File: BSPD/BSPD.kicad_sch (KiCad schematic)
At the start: 54 parts, among them J1 DT13-48PABCD-R015, K1 Latching Relay, Q2 STS6NF20V, Q3 STS6NF20V, U1 LM7805CT, U10 DK1A1B-12V, U12 OP AMP, U14 ISO1050DUB, U15 LM7809_TO220, U2 NSL-32, U2 OP AMP, U3 OP AMP, U4 NUCLEO-L432KC, U5 2x4 OR GATE, U6 LM555N, U8 NAND, U9 AND GATE

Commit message: Finished slug logo and shrunk pcb to size of components
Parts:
- removed SYM1: SYM_EasterEgg_42x60mm, 1FS_2_Global_Footprint_Library:FORMULA SLUG, symbol Graphic:SYM_EasterEgg_42x60mm
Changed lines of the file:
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@@
   (title_block
     (title "Brake System Plausability Device +")
-    (date "2024-02-22")
+    (date "2024-02-27")
     (rev "FS2 4.3")
   )
@@
     )
   )
+  (symbol (lib_id "1FS_2_Global_Symbol_Library:FS Logo") (at 535.94 44.45 0) (unit 1)
+    (in_bom yes) (on_board yes) (dnp no) (fields_autoplaced)
+    (property "Reference" "#G1" (at 535.94 19.685 0)
+      (effects (font (size 1.27 1.27)) hide)
+    )
+    (property "Value" "FS Logo" (at 535.94 69.215 0)
+      (effects (font (size 1.27 1.27)) hide)
+    )
+    (property "Footprint" "1FS_2_Global_Footprint_Library:FORMULA SLUG" (at 535.94 44.45 0)
+      (effects (font (size 1.27 1.27)) hide)
+    )
+    (property "Datasheet" "" (at 535.94 44.45 0)
+      (effects (font (size 1.27 1.27)) hide)
+    )
+    (instances
+      (project "BSPD"
+        (path "/9b958334-fa88-4811-8197-71444a07b1b5"
+          (reference "#G1") (unit 1)
+        )
+      )
+    )
+  )
   (symbol (lib_id "Device:R_US") (at 119.38 50.8 270) (unit 1)
     (in_bom yes) (on_board yes) (dnp no)
@@
         )
       )
-    )
-  )
-  (symbol (lib_id "Graphic:SYM_EasterEgg_42x60mm") (at 548.64 86.36 0) (unit 1)
-    (in_bom no) (on_board yes) (dnp no) (fields_autoplaced)
-    (property "Reference" "SYM1" (at 548.64 86.36 0)
-      (effects (font (size 1.27 1.27)) hide)
-    )
-    (property "Value" "SYM_EasterEgg_42x60mm" (at 548.64 86.36 0)
-      (effects (font (size 1.27 1.27)) hide)
-    )
-    (property "Footprint" "1FS_2_Global_Footprint_Library:FORMULA SLUG" (at 548.64 90.17 0)
-      (effects (font (size 1.27 1.27)) hide)
-    )
-    (property "Datasheet" "https://eur-lex.europa.eu/LexUriServ/LexUriServ.do?uri=OJ:L:2013:347:0671:0854:de:PDF" (at 548.64 92.71 0)
-      (effects (font (size 1.27 1.27)) hide)
-    )
-    (property "Sim.Enable" "0" (at 548.64 88.9 0)
-      (effects (font (size 1.27 1.27)) hide)
-    )
-    (instances
-      (project "BSPD"
-        (path "/9b958334-fa88-4811-8197-71444a07b1b5"
-          (reference "SYM1") (unit 1)
-        )
-      )

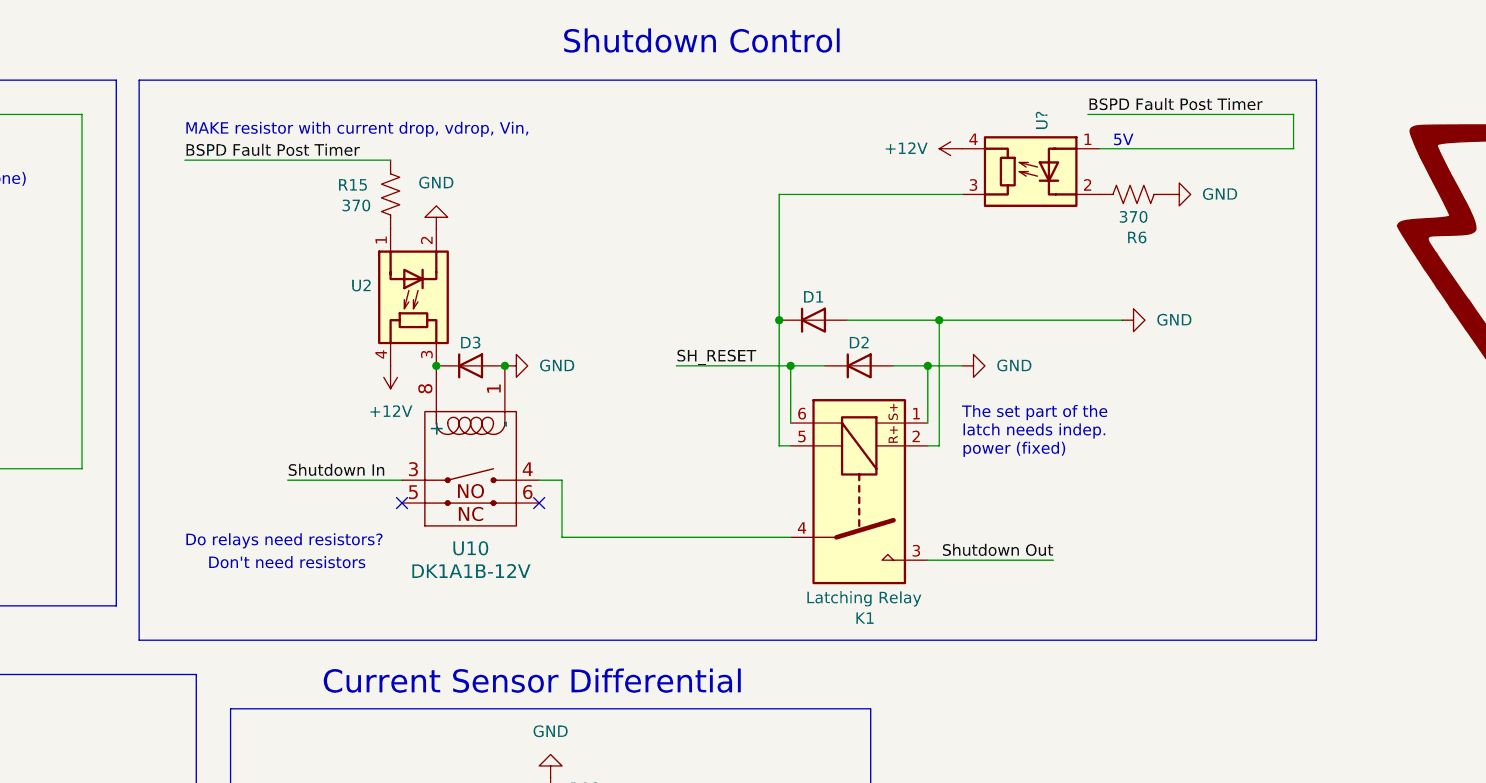
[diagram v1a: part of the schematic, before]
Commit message: Fixed stray traces, optocoupler pins, and opto library entry
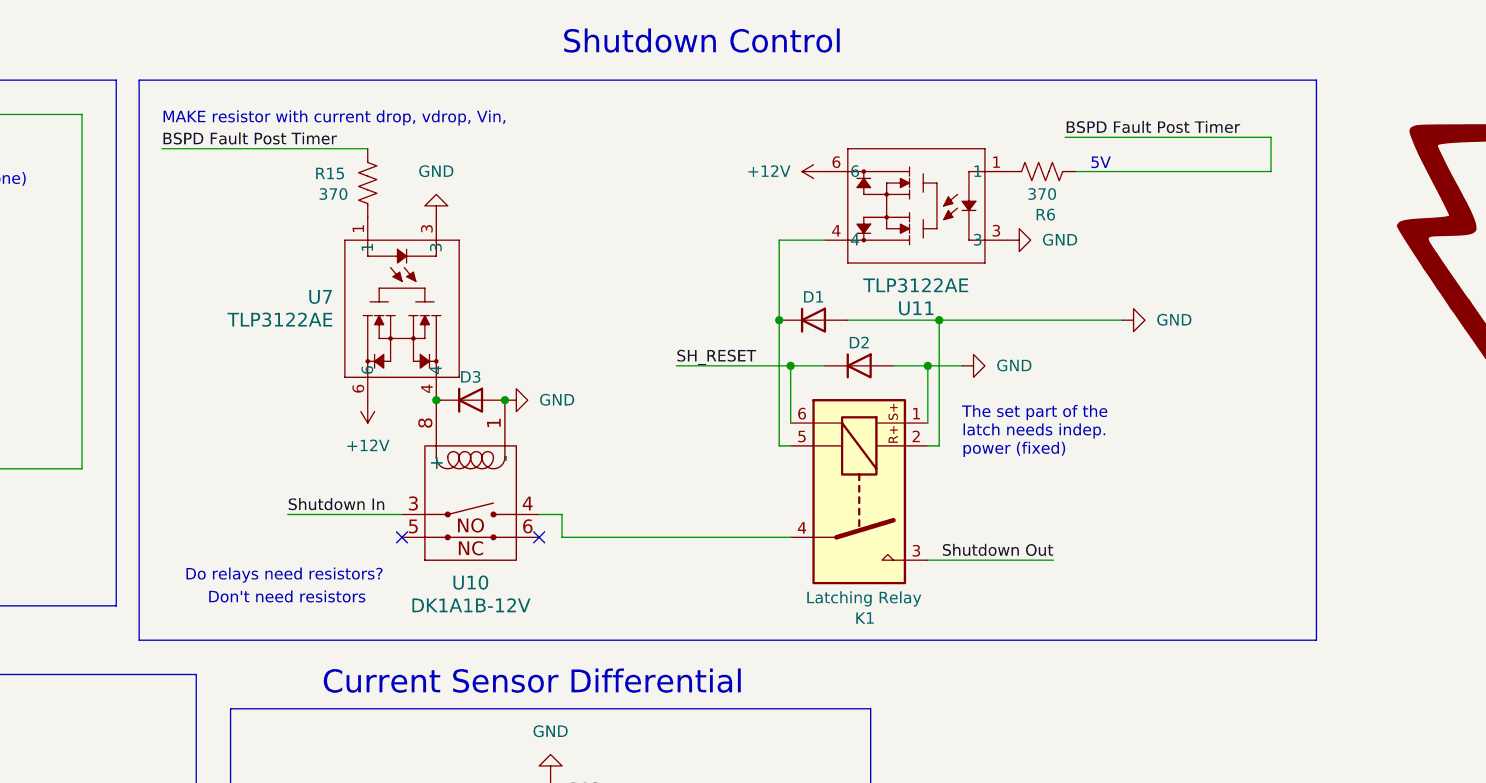
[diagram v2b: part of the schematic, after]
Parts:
- removed U2, U?: NSL-32, 1FS_2_Global_Footprint_Library:OptoCoupler 6-SOP, symbol Isolator:NSL-32
- added U11, U7: TLP3122AE, 1FS_2_Global_Footprint_Library:OptoCoupler 6-SOP, symbol 1FS_2_Global_Symbol_Library:TLP3122AE
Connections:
- net +12V: now also U11.6, U7.6
- net BSPD Fault Post Timer: now also R6.1
- net GND: now also U11.3, U7.3; no longer R6.1
- net at R15.1: now also U7.1
- net at D3.1 (K), U10.8 (+): now also U7.4
- net at D1.1 (K), K1.5: now also U11.4
- net at R6.2: now also U11.1
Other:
- moved on the sheet: D3, R15, R6, U10

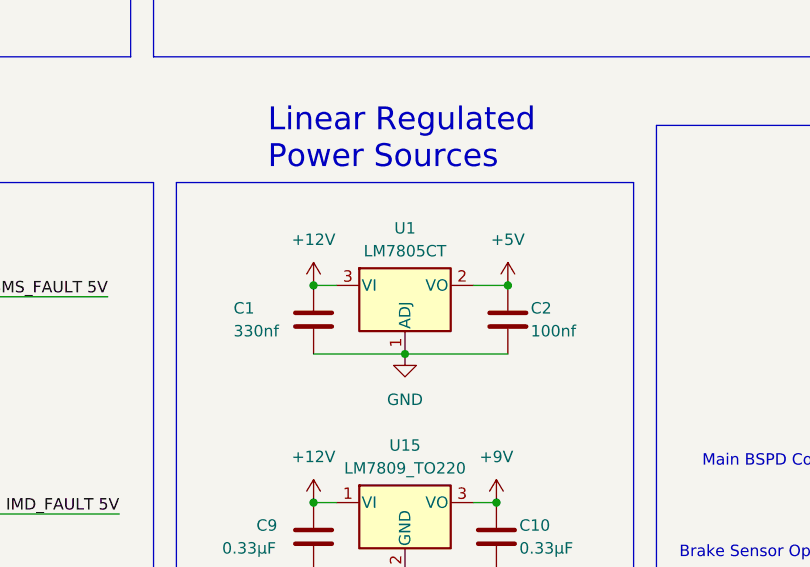
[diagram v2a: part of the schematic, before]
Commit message: fixed 5v lin reg pins and trace overlapping holes
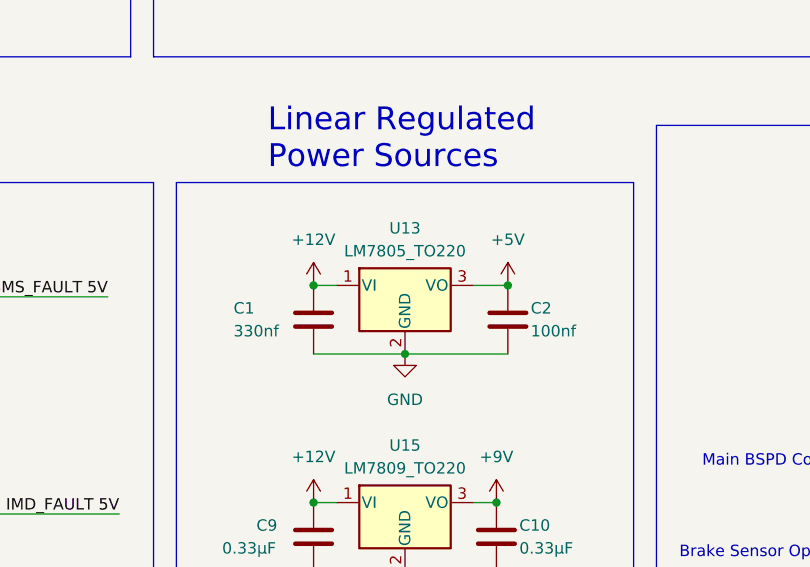
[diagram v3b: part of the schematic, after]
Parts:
- removed U1: LM7805CT, Package_TO_SOT_THT:TO-220-3_Vertical, symbol Regulator_Linear:LM317_TO-252
- added U13: LM7805_TO220, Package_TO_SOT_THT:TO-220-3_Vertical, symbol Regulator_Linear:LM7805_TO220
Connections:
- net +12V: now also U13.1 (VI)
- net +5V: now also U13.3 (VO)
- net GND: now also U13.2 (GND)

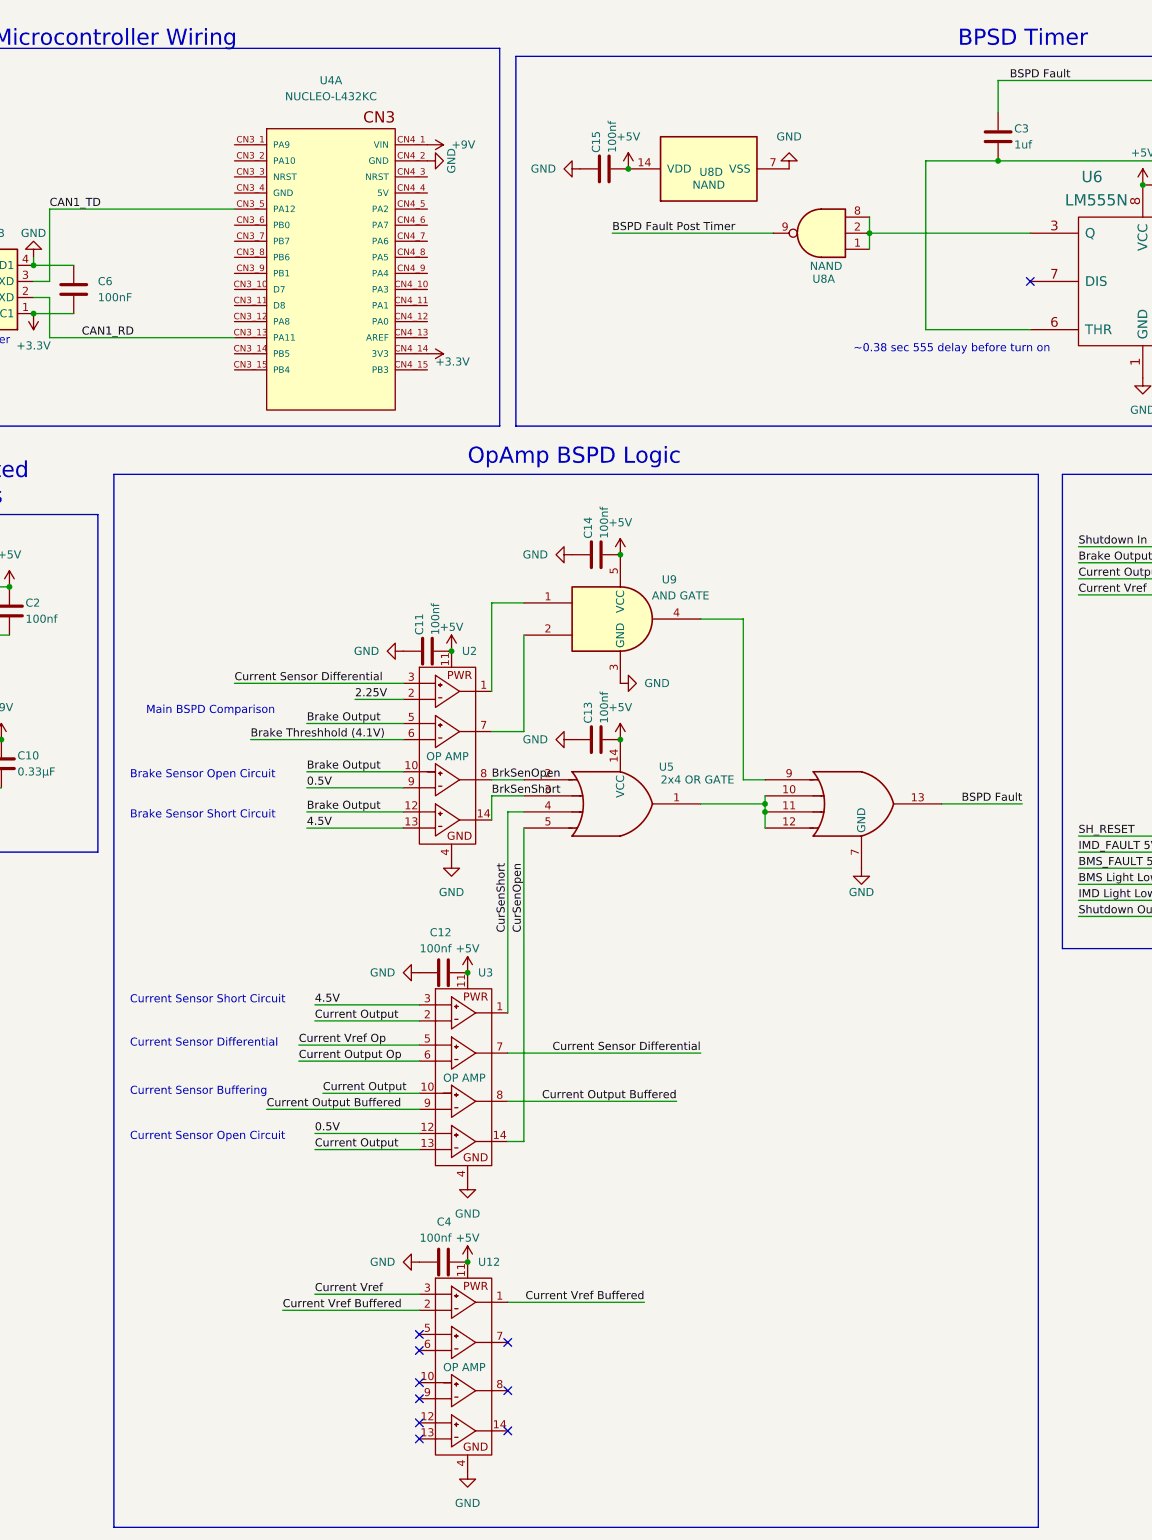
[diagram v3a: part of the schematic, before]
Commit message: fixed and/nand pins and packages
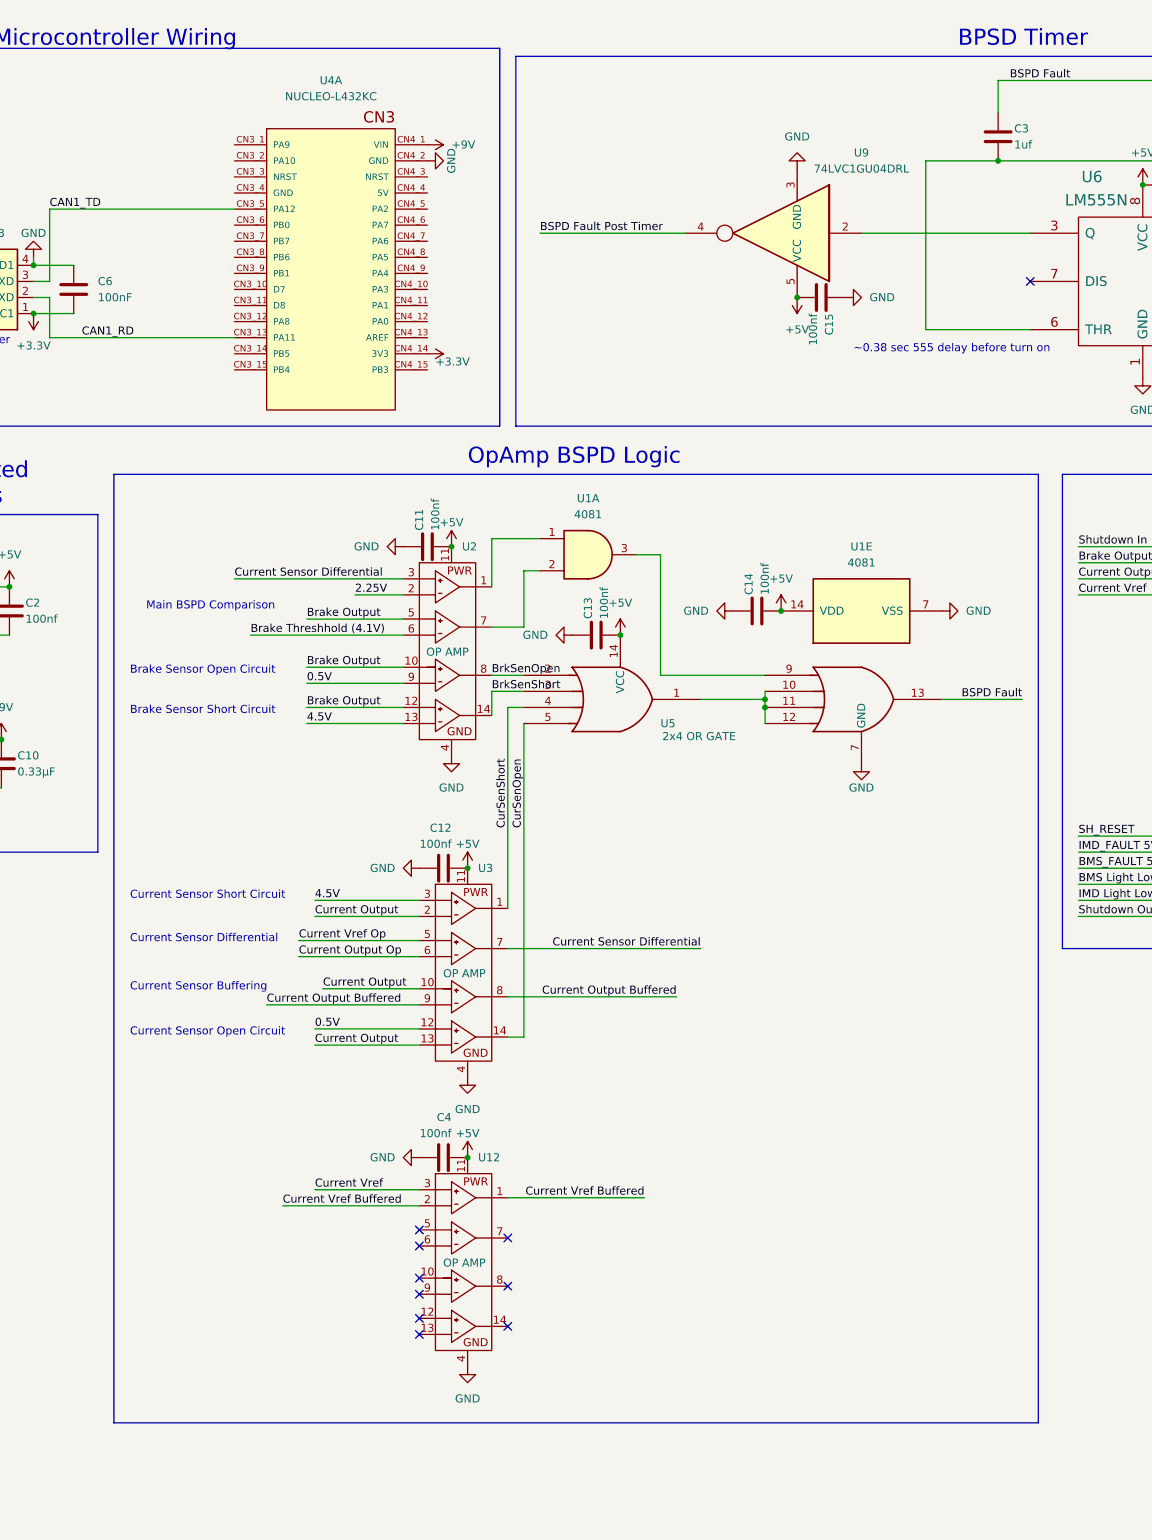
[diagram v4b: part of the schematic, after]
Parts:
- removed U8: NAND, Package_DIP:DIP-14_W7.62mm, symbol 4xxx:4023
- removed U9: AND GATE, Package_DIP:DIP-14_W7.62mm, symbol 74xGxx:74AHC1G08
- added U1: 4081, Package_SO:SOIC-14_3.9x8.7mm_P1.27mm, symbol 4xxx:4081
- added U9: 74LVC1GU04DRL, Package_TO_SOT_SMD:SOT-553, symbol 74xGxx:74LVC1GU04DRL
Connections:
- net +5V: now also U1.14 (VDD), U9.5 (VCC)
- net BSPD Fault Post Timer: now also U9.4
- net GND: now also U1.7 (VSS), U9.3 (GND)
- net at U6.3 (Q): now also U9.2
- net at U2.1: now also U1.1
- net at U2.7: now also U1.2
- net at U5.9: now also U1.3
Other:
- moved on the sheet: C11, C12, C13, C14, C15, C4, U12, U2, U3, U5

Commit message: Fixed minor schematic bits
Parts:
- C10, C9: value 0.33µF -> 0.33µf
- C5, C6: value 100nF -> 100nf

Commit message: more minor changes to schematic
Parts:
- C10, C9: value 0.33µf -> 330nf

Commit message: more small changes
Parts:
- C10: value 330nf -> 100nf

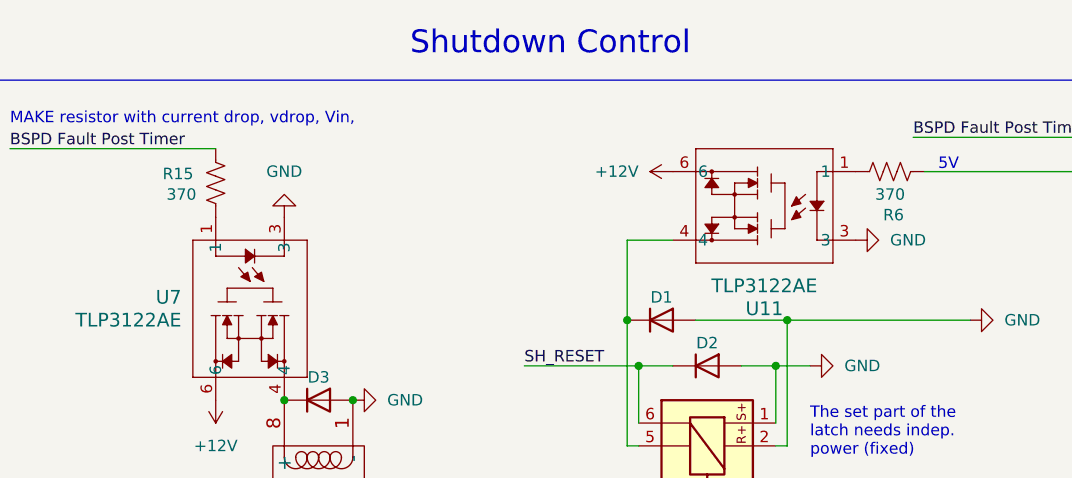
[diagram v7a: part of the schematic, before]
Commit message: updated opto res #s
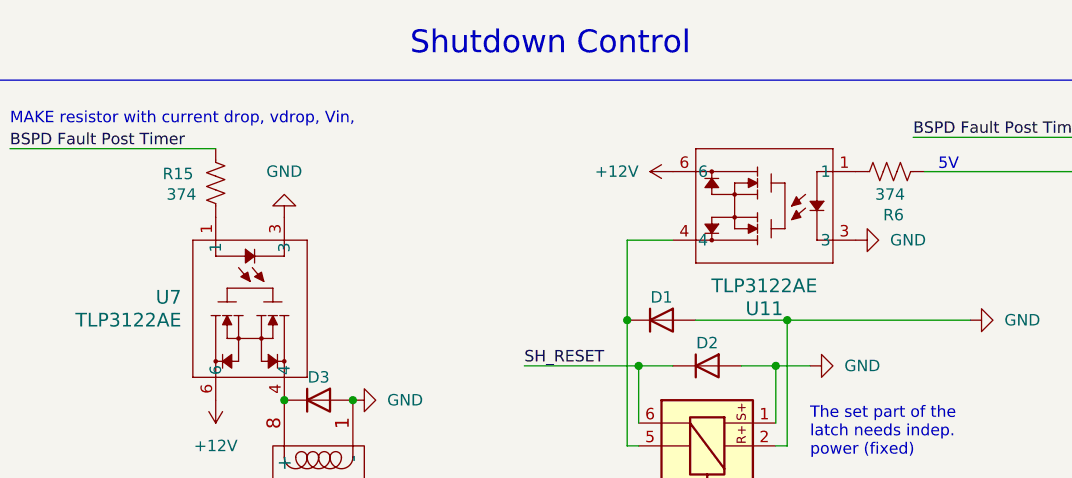
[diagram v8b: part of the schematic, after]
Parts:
- R15, R6: value 370 -> 374
